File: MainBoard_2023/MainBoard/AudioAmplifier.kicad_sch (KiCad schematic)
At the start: 21 parts, among them J6 Conn_01x02, J7 Conn_01x02, U7 YDA142

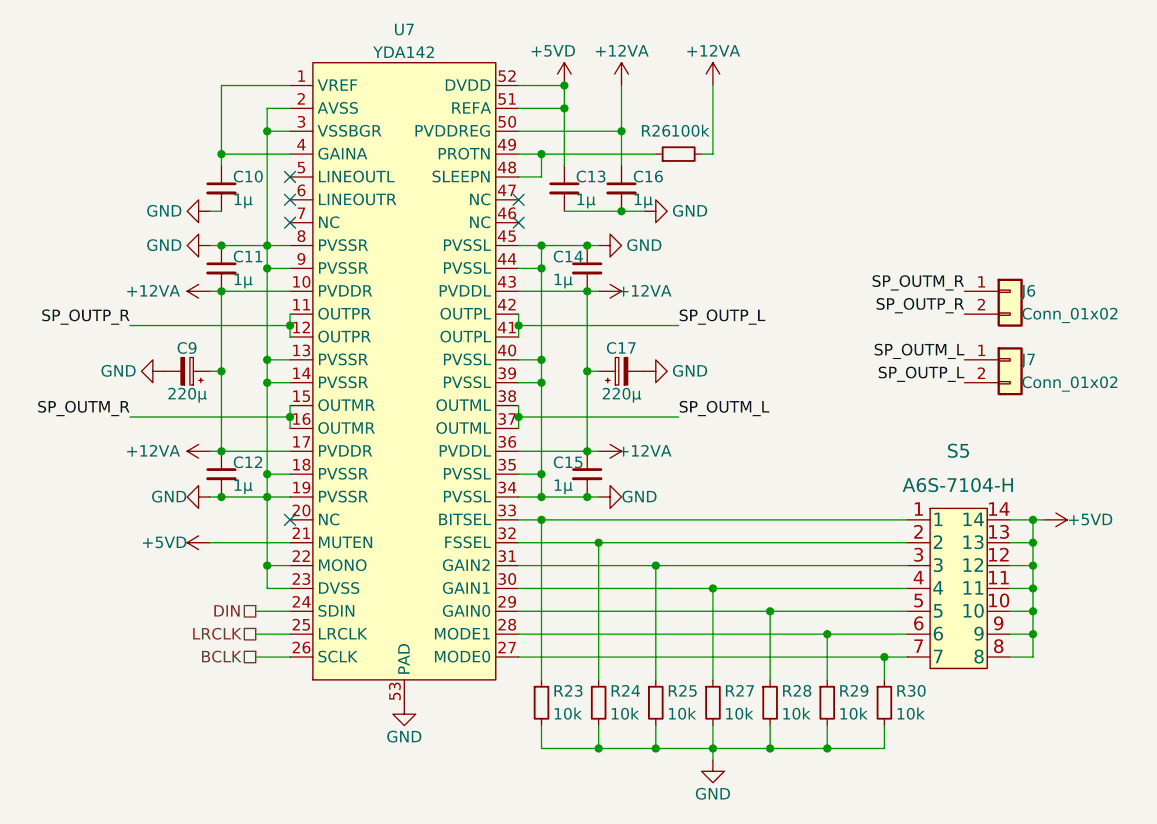
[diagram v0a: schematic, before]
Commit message: アンプのGNDをGNDAに変更
GNDAとGNDをブロックタイプエミフィルとコモンモードチョークでアイソレート
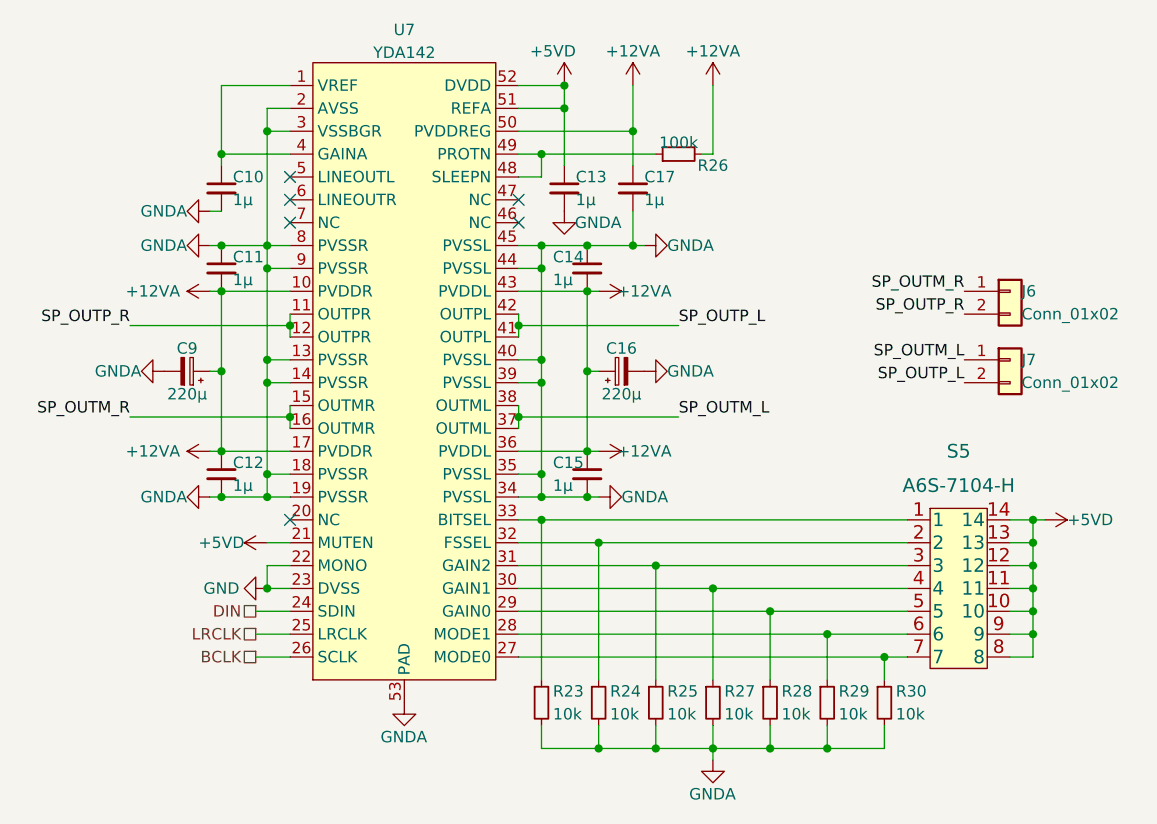
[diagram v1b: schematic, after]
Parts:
- renumbered C17 to C16, C16 to C17
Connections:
- net GND: no longer C10.2, C11.1, C12.2, C13.2, C14.1, C15.2, C16.2, C17.2, C9.2, R23.2, R24.2, R25.2, R27.2, R28.2, R29.2, R30.2, U7.13 (PVSSR), U7.14 (PVSSR), U7.18 (PVSSR), U7.19 (PVSSR), U7.2 (AVSS), U7.3 (VSSBGR), U7.34 (PVSSL), U7.35 (PVSSL), U7.39 (PVSSL), U7.40 (PVSSL), U7.44 (PVSSL), U7.45 (PVSSL), U7.53 (PAD), U7.8 (PVSSR), U7.9 (PVSSR)
- new net GNDA: C10.2, C11.1, C12.2, C13.2, C14.1, C15.2, C16.2, C17.2, C9.2, R23.2, R24.2, R25.2, R27.2, R28.2, R29.2, R30.2, U7.13 (PVSSR), U7.14 (PVSSR), U7.18 (PVSSR), U7.19 (PVSSR), U7.2 (AVSS), U7.3 (VSSBGR), U7.34 (PVSSL), U7.35 (PVSSL), U7.39 (PVSSL), U7.40 (PVSSL), U7.44 (PVSSL), U7.45 (PVSSL), U7.53 (PAD), U7.8 (PVSSR), U7.9 (PVSSR)
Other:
- moved on the sheet: C17
